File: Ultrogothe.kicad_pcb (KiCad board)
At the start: 4 copper layers, 20.3 x 54.6 mm, 24 parts, among them J1 Conn_01x20, J2 Conn_01x20, J3 Conn_02x05_Top_Bottom, U1 XC6206PxxxMR, U2 STM32F103CBTx, Y1 Crystal

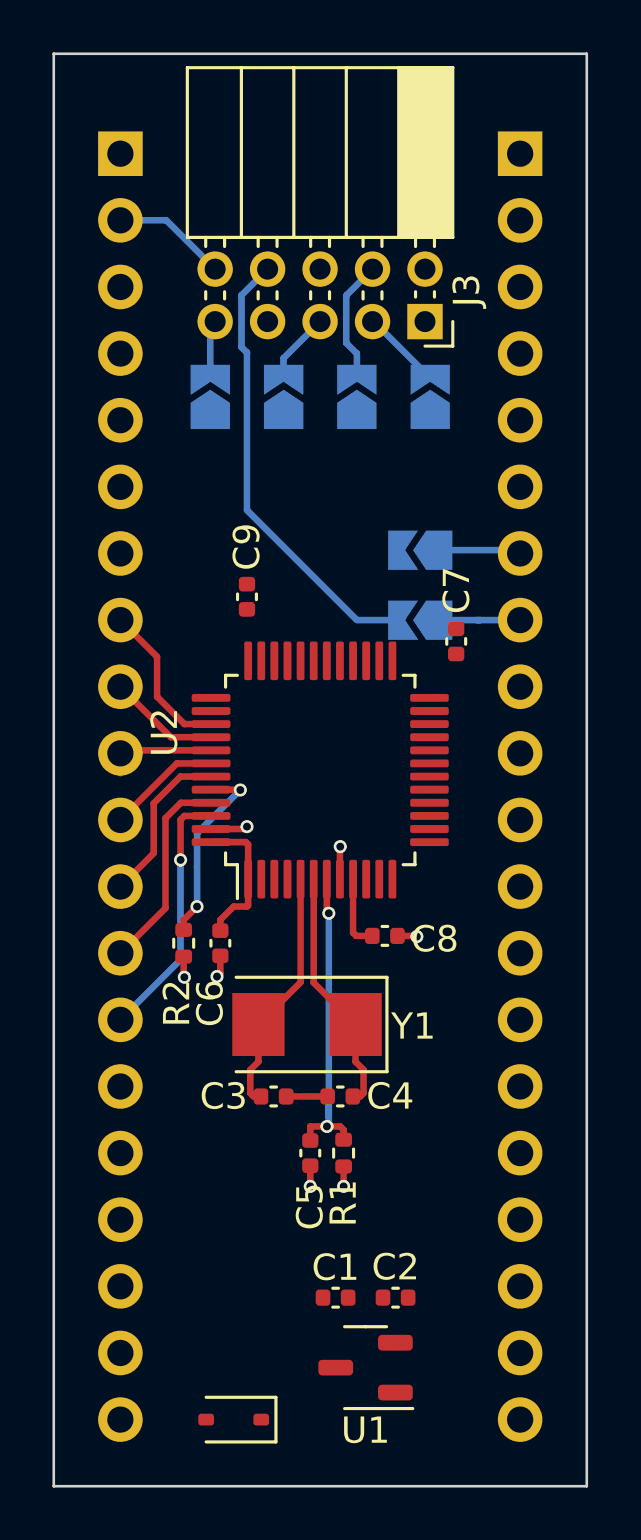
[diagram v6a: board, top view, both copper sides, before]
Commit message: répartition pins et routage
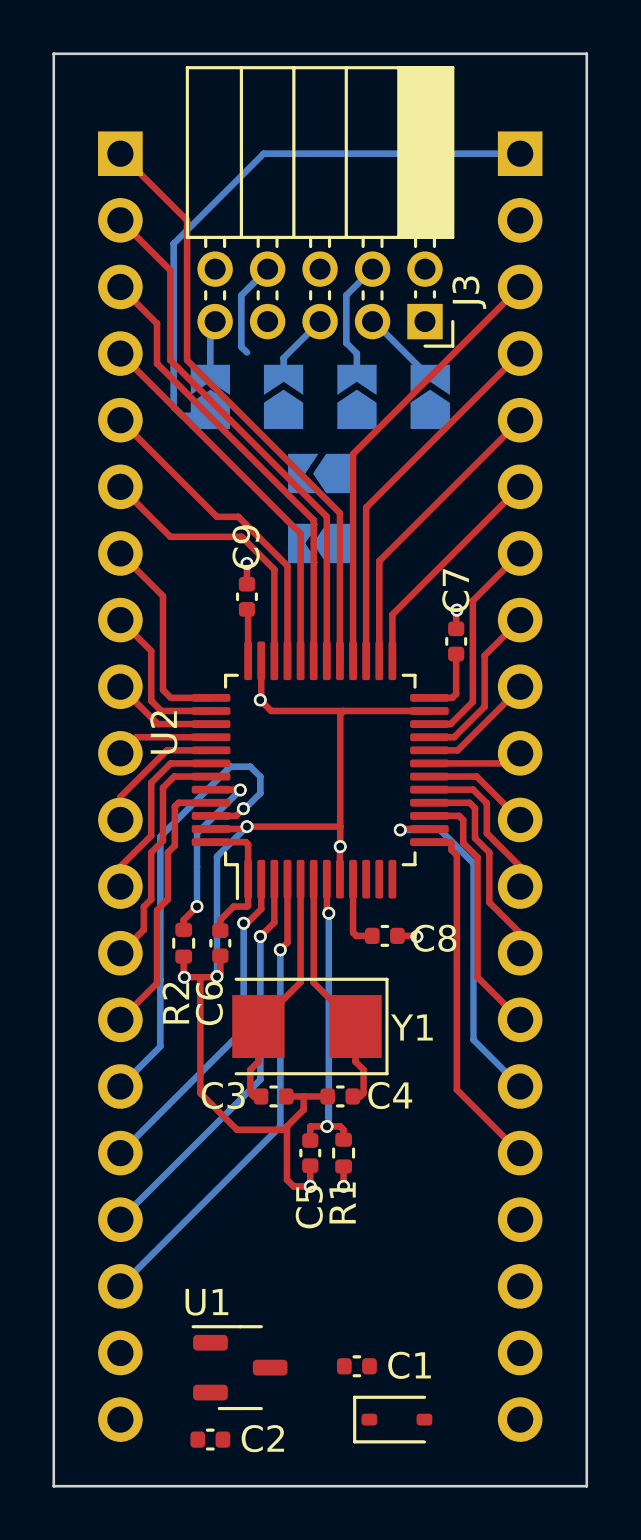
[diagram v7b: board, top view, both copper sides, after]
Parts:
- moved C2 8.90 mm to (130.4, 99.8), turned to 180 degrees
- moved D1 6.22 mm to (137.5, 99.1), turned to 0 degrees
- moved JP3 4.80 mm to (134.6, 63.0)
- moved JP6 4.80 mm to (134.6, 65.7)
- moved U1 4.78 mm to (131.6, 97.1), turned to 0 degrees
- moved C1 2.74 mm to (136.0, 97.0)
- moved Y1 0.08 mm to (134.1, 84.1)
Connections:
- J1 pad 1: 5Vext -> A8
- J1 pad 10: B5 -> B4
- J1 pad 11: B6 -> B5
- J1 pad 12: B7 -> B6
- J1 pad 13: B8 -> B7
- J1 pad 14: B9 -> B8
- J1 pad 15: B10 -> B9
- J1 pad 16: B11 -> C13
- J1 pad 17: B12 -> C14
- J1 pad 18: B13 -> C15
- J1 pad 19: B14 -> 0V
- J1 pad 2: 3V3 -> A9
- J1 pad 20: B15 -> 3V3
- J1 pad 3: 0V -> A10
- J1 pad 4: nRST -> A11
- J1 pad 5: B0 -> A12
- J1 pad 6: B1 -> A13
- J1 pad 7: B2 -> A14
- J1 pad 8: B3 -> A15
- J1 pad 9: B4 -> B3
- J2 pad 1: unconnected-(J2-Pin_1-Pad1) -> nRST
- J2 pad 10: A5 -> B1
- J2 pad 11: A6 -> B0
- J2 pad 13: A8 -> A6
- J2 pad 14: A9 -> A5
- J2 pad 15: A10 -> A4
- J2 pad 16: A11 -> A3
- J2 pad 17: A12 -> A2
- J2 pad 18: A13 -> A1
- J2 pad 19: A14 -> A0
- J2 pad 2: C13 -> unconnected-(J2-Pin_2-Pad2)
- J2 pad 20: A15 -> 5Vext
- J2 pad 3: C14 -> B15
- J2 pad 4: C15 -> B14
- J2 pad 5: A0 -> B13
- J2 pad 6: A1 -> B12
- J2 pad 7: A2 -> B11
- J2 pad 8: A3 -> B10
- J2 pad 9: A4 -> B2
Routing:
- net 0V: track 7.41 -> 46.0 mm, vias 6 -> 9
- net A8: track 0.00 -> 22.8 mm
- net nRST: track 12.2 -> 34.6 mm
- net A9: track 0.00 -> 20.1 mm
- net C15: track 0.00 -> 18.2 mm, vias 0 -> 1
- net A10: track 0.00 -> 17.3 mm
- net B15: track 0.00 -> 16.9 mm
- net C14: track 0.00 -> 15.4 mm, vias 0 -> 1
- net A11: track 0.00 -> 14.6 mm
- net B14: track 0.00 -> 14.1 mm
- net A4: track 0.00 -> 13.7 mm, vias 0 -> 1
- net /s_debugger/T_TX: track 17.3 -> 3.68 mm
- net C13: track 0.00 -> 12.7 mm, vias 0 -> 1
- net A12: track 0.00 -> 12.3 mm
- net B13: track 0.00 -> 11.4 mm
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
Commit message: routage fini
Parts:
- removed JP1, JP2, JP3, JP4, JP5, JP6: SolderJumper_2_Open, Jumper:SolderJumper-2_P1.3mm_Open_TrianglePad1.0x1.5mm
- J3: value Conn_02x05_Top_Bottom -> Conn_02x05_Odd_Even
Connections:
- J3 pad 2: unconnected-(J3-Pin_2-Pad2) -> 0V
- J3 pad 3: /s_debugger/T_DIO -> unconnected-(J3-Pin_3-Pad3)
- J3 pad 4: /s_debugger/T_CLK -> A2
- J3 pad 5: /s_debugger/T_SWO -> A13
- J3 pad 6: 0V -> A3
- J3 pad 7: /s_debugger/T_RX -> A14
- J3 pad 8: /s_debugger/T_TX -> nRST
- J3 pad 9: /s_debugger/T_RST -> A8
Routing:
- net 0V: track 46.0 -> 124.0 mm, vias 9 -> 153
- net 3V3: track 13.6 -> 86.7 mm, vias 1 -> 6
- net A2: track 0.00 -> 41.2 mm, vias 0 -> 1
- net A3: track 13.8 -> 38.3 mm, vias 0 -> 1
- net A0: track 0.00 -> 20.5 mm, vias 0 -> 1
- net A1: track 0.00 -> 20.1 mm, vias 0 -> 1
- net nRST: track 34.6 -> 53.9 mm
- net A13: track 10.7 -> 29.4 mm, vias 0 -> 1
- net A14: track 7.84 -> 21.8 mm, vias 0 -> 1
- net /s_debugger/5V: track 0.00 -> 6.46 mm
- net A8: track 22.8 -> 28.9 mm
- net /s_debugger/T_CLK: track 4.73 -> 0.00 mm
- net /s_debugger/T_TX: track 3.68 -> 0.00 mm
- net 5Vext: track 0.00 -> 3.65 mm
- net /s_debugger/T_DIO: track 3.09 -> 0.00 mm
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- added copper zone on B.Cu, net 0V
- added copper zone on F.Cu, net 0V
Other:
- copper layers 4 -> 2
- board text added: "0V"
- board text added: "3V3"
- board text added: "RST"
- board text added: "T_CLK"
- board text added: "T_DIO"
- board text added: "T_RX"
- board text added: "T_SWO"
- board text added: "T_TX"
- board text added: "Ultrogothe 2024/07/31"
- board text added: "libre"
